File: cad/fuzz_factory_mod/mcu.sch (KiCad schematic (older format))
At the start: 3 parts

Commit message: Continued schematic.
Modified fuuz_factory circuit : use of matched transistor pairs.
Added USB interface, through FT230X and direct to MCU.
Associated footprints, except for XTAL and trimmers.
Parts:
- removed P? (x2): CONN_NUCLEO_L152RE, symbol flax_lib:CONN_NUCLEO_L152RE
- removed R?: R, symbol Device:R
- added C201, C209: 1u, Capacitors_SMD:C_0805, symbol Device:C
- added C202, C208: 10n, Capacitors_SMD:C_0603, symbol Device:C
- added C203: 4u7, Capacitors_SMD:C_1206, symbol Device:C
- added C204, C205, C206, C207: 100n, Capacitors_SMD:C_0603, symbol Device:C
- added J201: Conn_MCU_SWD, Pin_Headers:Pin_Header_Straight_1x07_Pitch2.54mm, symbol Connector:Conn_01x07_Male
- added L201: BLMxxx, Capacitors_SMD:C_0603, symbol Device:L
- added R201: 10k, Resistors_SMD:R_0603, symbol Device:R_Small
- added R202: 390, Resistors_SMD:R_0603, symbol Device:R_Small
- added R203: 1M, Resistors_SMD:R_0603, symbol Device:R_Small
- added U201: STM32F303VCTx, Housings_QFP:LQFP-100_14x14mm_Pitch0.5mm, symbol MCU_ST_STM32F3:STM32F303VCTx
- added Y201: Resonator_Small, symbol Device:Resonator_Small
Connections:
- net labels added: +3.3VA, ADC1_IN1, ADC1_IN2, ADC1_IN3, ADC1_IN4, ADC1_IN5, ADC2_IN5, ADC2_IN6, ADC2_IN7, ADC2_IN8, ADC2_IN9, ADC_FF_pol1, ADC_FF_pol2, ADC_FF_pol3, ADC_Peak_input, ADC_Peak_output, ADC_Ref_pol1, ADC_Ref_pol2, ADC_Ref_pol3, DAC_OUT1, ENC1_BTN, ENC1_IN_CCW, ENC1_IN_CW, ENC1_LED_BLUE, ENC1_LED_GREEN, ENC1_LED_RED, ENC2_BTN, ENC2_IN_CCW, ENC2_IN_CW, ENC2_LED_BLUE, ENC2_LED_GREEN, ENC2_LED_RED, FF_Stab_DAC_PWM, GNDA, JNTRST, JTCK_SWCLK, JTDI, JTDO_TRACESWO, JTMS_SWDIO, LED_BYPASS, LED_BYPASS_CMD, MUX1, MUX2, MUX3, Ref_Stab_DAC_PWM, SPI1_CS, SPI1_MISO, SPI1_MOSI, SPI1_SCK, SPI2_MISO, SPI2_MOSI, SPI2_NSS, SPI2_SCK, SPI3_MOSI, SPI3_SCK, SPI_FF_Gain_CS, SPI_FF_Gain_MISO, SPI_FF_Gain_MOSI, SPI_FF_Gain_SCK, SW_BYPASS, SW_PRESET_DOWN, SW_PRESET_UP, TIM1_CH1, TIM1_CH2, TIM3_CH1, TIM3_CH2, TIM4_CH1, UART3_RX, UART3_TX, UART5_RX, UART5_TX, USART1_RX, USB_DM, USB_DP, VCA_IN_PWM, VCA_OUT_PWM
- net labels removed: +5V, +9V
- wire segments 11 -> 131

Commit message: Continued schematic.
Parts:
- Y201: footprint (none) -> Pin_Headers:Pin_Header_Straight_1x03_Pitch2.54mm
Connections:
- net labels added: FF_Stab_DAC_PWM_LSB, FF_Stab_DAC_PWM_MSB, Ref_Stab_DAC_PWM_LSB, Ref_Stab_DAC_PWM_MSB, TIM1_CH3, TIM1_CH4
- net labels removed: FF_Stab_DAC_PWM, Ref_Stab_DAC_PWM
- wire segments 131 -> 145
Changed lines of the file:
@@
 $Descr A4 11693 8268
 encoding utf-8
-Sheet 2 22
+Sheet 2 26
 Title ""
 Date ""
@@
 F 0 "Y201" V 2645 2600 50  0000 C CNN
 F 1 "Resonator_Small" V 2736 2600 50  0000 C CNN
-F 2 "" H 2925 2650 50  0001 C CNN
+F 2 "Pin_Headers:Pin_Header_Straight_1x03_Pitch2.54mm" H 2925 2650 50  0001 C CNN
 F 3 "~" H 2925 2650 50  0001 C CNN
 	1    2950 2650
@@
 Text GLabel 2500 3550 0    50   Input ~ 0
 SW_PRESET_DOWN
-Text GLabel 2500 3850 0    50   Input ~ 0
-ENC1_LED_RED
-Text GLabel 2500 3950 0    50   Input ~ 0
-ENC1_LED_GREEN
-Text GLabel 2500 4050 0    50   Input ~ 0
-ENC1_LED_BLUE
-Text GLabel 2500 5450 0    50   Input ~ 0
-ENC2_LED_RED
-Text GLabel 2500 5550 0    50   Input ~ 0
-ENC2_LED_GREEN
-Text GLabel 2500 5650 0    50   Input ~ 0
-ENC2_LED_BLUE
-Text GLabel 2500 5750 0    50   Input ~ 0
-ENC2_BTN
-Text GLabel 2500 5850 0    50   Input ~ 0
-ENC2_IN_CW
-Text GLabel 6500 6550 2    50   Input ~ 0
-ENC1_IN_CW
-Text GLabel 6500 6650 2    50   Input ~ 0
-ENC1_IN_CCW
-Text GLabel 6500 6450 2    50   Input ~ 0
-ENC1_BTN
-Text GLabel 6500 4050 2    50   Input ~ 0
-ENC2_IN_CCW
 Text GLabel 2500 3650 0    50   Input ~ 0
 VCA_IN_PWM
@@
 VCA_OUT_PWM
 Text GLabel 2500 4350 0    50   Input ~ 0
-FF_Stab_DAC_PWM
-Text GLabel 2500 4550 0    50   Input ~ 0
-Ref_Stab_DAC_PWM
+FF_Stab_DAC_PWM_LSB
+Text GLabel 2500 4750 0    50   Input ~ 0
+Ref_Stab_DAC_PWM_LSB
 $Sheet
-S 9950 4250 800  300
+S 10200 5600 800  300
 U 5EB00B3E
 F0 "USB_UART" 50
 F1 "USB_UART.sch" 50
-F2 "USB_RXD" I L 9950 4350 50
-F3 "USB_TXD" I L 9950 4450 50
+F2 "USB_RXD" I L 10200 5700 50
+F3 "USB_TXD" I L 10200 5800 50
 $EndSheet
 $Sheet
-S 9950 3650 800  300
+S 10200 5000 800  300
 U 5EB591ED
 F0 "USB_DEV" 50
 F1 "USB_DEV.sch" 50
-F2 "USB_DM" I L 9950 3750 50
-F3 "USB_DP" I L 9950 3850 50
+F2 "USB_DM" I L 10200 5100 50
+F3 "USB_DP" I L 10200 5200 50
 $EndSheet
-Text GLabel 9800 3750 0    50   Input ~ 0
+Text GLabel 10050 5100 0    50   Input ~ 0
 USB_DM
-Text GLabel 9800 3850 0    50   Input ~ 0
+Text GLabel 10050 5200 0    50   Input ~ 0
 USB_DP
 Wire Wire Line
-	9800 3750 9950 3750
-Wire Wire Line
-	9950 3850 9800 3850
+	10050 5100 10200 5100
+Wire Wire Line
+	10200 5200 10050 5200
+Text Label 3650 4750 2    50   ~ 0
+TIM1_CH3
+Text Label 3650 4850 2    50   ~ 0
+TIM1_CH4
+Wire Wire Line
+	3750 4750 2500 4750
+Wire Wire Line
+	3750 4850 2500 4850
+Text GLabel 2500 4550 0    50   Input ~ 0
+FF_Stab_DAC_PWM_MSB
+Text GLabel 2500 4850 0    50   Input ~ 0
+Ref_Stab_DAC_PWM_MSB
+$Sheet
+S 10000 1500 1000 2500
+U 5EEFDD5E
+F0 "interface" 50
+F1 "interface.sch" 50
+F2 "DISP_CLK" I L 10000 1600 50
+F3 "DISP_DATA" I L 10000 1700 50
+F4 "DISP_ENABLE" I L 10000 1800 50
+F5 "DISP_LATCH" I L 10000 1900 50
+F6 "ENC1_SW" I L 10000 2050 50
+F7 "ENC1_LED1" I L 10000 2150 50
+F8 "ENC1_LED2" I L 10000 2250 50
+F9 "ENC1_ENC1" I L 10000 2350 50
+F10 "ENC1_ENC2" I L 10000 2450 50
+F11 "FSW_bypass" I L 10000 3700 50
+F12 "ENC2_SW" I L 10000 2600 50
+F13 "ENC2_LED1" I L 10000 2700 50
+F14 "ENC2_LED2" I L 10000 2800 50
+F15 "ENC2_ENC1" I L 10000 2900 50
+F16 "ENC2_ENC2" I L 10000 3000 50
+F17 "ENC3_SW" I L 10000 3150 50
+F18 "ENC3_LED1" I L 10000 3250 50
+F19 "ENC3_LED2" I L 10000 3350 50
+F20 "ENC3_ENC1" I L 10000 3450 50
+F21 "ENC3_ENC2" I L 10000 3550 50
+$EndSheet
+Text Label 9900 1600 2    50   ~ 0
+SPI2_SCK
+Text Label 9900 1700 2    50   ~ 0
+SPI2_MOSI
+Wire Wire Line
+	10000 1600 9500 1600
+Wire Wire Line
+	10000 1700 9500 1700
+Text Label 9900 2700 2    50   ~ 0
+ENC2_LED_RED
+Text Label 9900 2800 2    50   ~ 0
+ENC2_LED_GREEN
+Text Label 9900 2600 2    50   ~ 0
+ENC2_BTN
+Text Label 9900 2900 2    50   ~ 0
+ENC2_IN_CW
+Text Label 9900 2050 2    50   ~ 0
+ENC1_BTN
+Text Label 9900 2350 2    50   ~ 0
+ENC1_IN_CW
+Text Label 9900 2450 2    50   ~ 0
+ENC1_IN_CCW
+Text Label 9900 2150 2    50   ~ 0
+ENC1_LED_RED
+Text Label 9900 2250 2    50   ~ 0
+ENC1_LED_GREEN
+Text Label 9900 3000 2    50   ~ 0
+ENC2_IN_CCW
+Wire Wire Line
+	10000 2050 9500 2050
+Wire Wire Line
+	10000 2150 9500 2150
+Wire Wire Line
+	10000 2250 9500 2250
+Wire Wire Line
+	10000 2350 9500 2350
+Wire Wire Line
+	10000 2450 9500 2450
+Wire Wire Line
+	10000 2600 9500 2600
+Wire Wire Line
+	10000 2700 9500 2700
+Wire Wire Line
+	10000 2800 9500 2800
+Wire Wire Line
+	10000 2900 9500 2900
+Wire Wire Line
+	10000 3000 9500 3000
 $EndSCHEMATC

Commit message: Continued schematic.
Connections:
- net labels added: BYPASS_CMD
- net labels removed: LED_BYPASS, LED_BYPASS_CMD
- wire segments 145 -> 153
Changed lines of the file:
@@
 $Descr A4 11693 8268
 encoding utf-8
-Sheet 2 26
+Sheet 2 30
 Title ""
 Date ""
@@
 	6500 5450 5350 5450
 Text Label 3650 3250 2    50   ~ 0
-LED_BYPASS
+BYPASS_CMD
 Wire Wire Line
 	3750 3250 2500 3250
@@
 Text GLabel 6500 3450 2    50   Input ~ 0
 SPI_FF_Gain_CS
-Text GLabel 2500 3150 0    50   Input ~ 0
-SW_BYPASS
 Text GLabel 2500 3250 0    50   Input ~ 0
-LED_BYPASS_CMD
-Text GLabel 2500 3450 0    50   Input ~ 0
-SW_PRESET_UP
-Text GLabel 2500 3550 0    50   Input ~ 0
-SW_PRESET_DOWN
+BYPASS_CMD
 Text GLabel 2500 3650 0    50   Input ~ 0
 VCA_IN_PWM
@@
 Wire Wire Line
 	10000 3000 9500 3000
+$Sheet
+S 10000 4250 1000 500
+U 5ECAAB94
+F0 "MIDI" 50
+F1 "MIDI.sch" 50
+F2 "MIDI_IN" I L 10000 4350 50
+F3 "MIDI_OUT" I L 10000 4650 50
+$EndSheet
+Text Label 9900 4350 2    50   ~ 0
+UART5_RX
+Text Label 9900 4650 2    50   ~ 0
+UART5_TX
+Wire Wire Line
+	10000 4350 9500 4350
+Wire Wire Line
+	10000 4650 9500 4650
+$Sheet
+S 8300 4700 700  300
+U 5ED0E0D0
+F0 "btn_bypass" 50
+F1 "push_button.sch" 50
+F2 "BTN" I L 8300 4900 50
+F3 "VCC" I L 8300 4800 50
+$EndSheet
+$Comp
+L power:+3.3V #PWR0229
+U 1 1 5ED10A5A
+P 8200 4800
+F 0 "#PWR0229" H 8200 4650 50  0001 C CNN
+F 1 "+3.3V" V 8215 4928 50  0000 L CNN
+F 2 "" H 8200 4800 50  0001 C CNN
+F 3 "" H 8200 4800 50  0001 C CNN
+	1    8200 4800
+	0    -1   -1   0
+$EndComp
+Wire Wire Line
+	8300 4800 8200 4800
+Text Label 8200 4900 2    50   ~ 0
+SW_BYPASS
+Wire Wire Line
+	8300 4900 7800 4900
+Text Label 8200 5400 2    50   ~ 0
+SW_PRESET_UP
+$Sheet
+S 8300 5200 700  300
+U 5ED20AFC
+F0 "btn_preset_up" 50
+F1 "push_button.sch" 50
+F2 "BTN" I L 8300 5400 50
+F3 "VCC" I L 8300 5300 50
+$EndSheet
+$Sheet
+S 8300 5700 700  300
+U 5ED214FE
+F0 "btn_preset_down" 50
+F1 "push_button.sch" 50
+F2 "BTN" I L 8300 5900 50
+F3 "VCC" I L 8300 5800 50
+$EndSheet
+Text Label 8200 5900 2    50   ~ 0
+SW_PRESET_DOWN
+Wire Wire Line
+	8300 5400 7500 5400
+Wire Wire Line
+	8300 5900 7500 5900
+$Comp
+L power:+3.3V #PWR0230
+U 1 1 5ED48B6A
+P 8200 5300
+F 0 "#PWR0230" H 8200 5150 50  0001 C CNN
+F 1 "+3.3V" V 8215 5428 50  0000 L CNN
+F 2 "" H 8200 5300 50  0001 C CNN
+F 3 "" H 8200 5300 50  0001 C CNN
+	1    8200 5300
+	0    -1   -1   0
+$EndComp
+$Comp
+L power:+3.3V #PWR0231
+U 1 1 5ED48FD7
+P 8200 5800
+F 0 "#PWR0231" H 8200 5650 50  0001 C CNN
+F 1 "+3.3V" V 8215 5928 50  0000 L CNN
+F 2 "" H 8200 5800 50  0001 C CNN
+F 3 "" H 8200 5800 50  0001 C CNN
+	1    8200 5800
+	0    -1   -1   0
+$EndComp
+Wire Wire Line
+	8300 5800 8200 5800
+Wire Wire Line
+	8300 5300 8200 5300
 $EndSCHEMATC

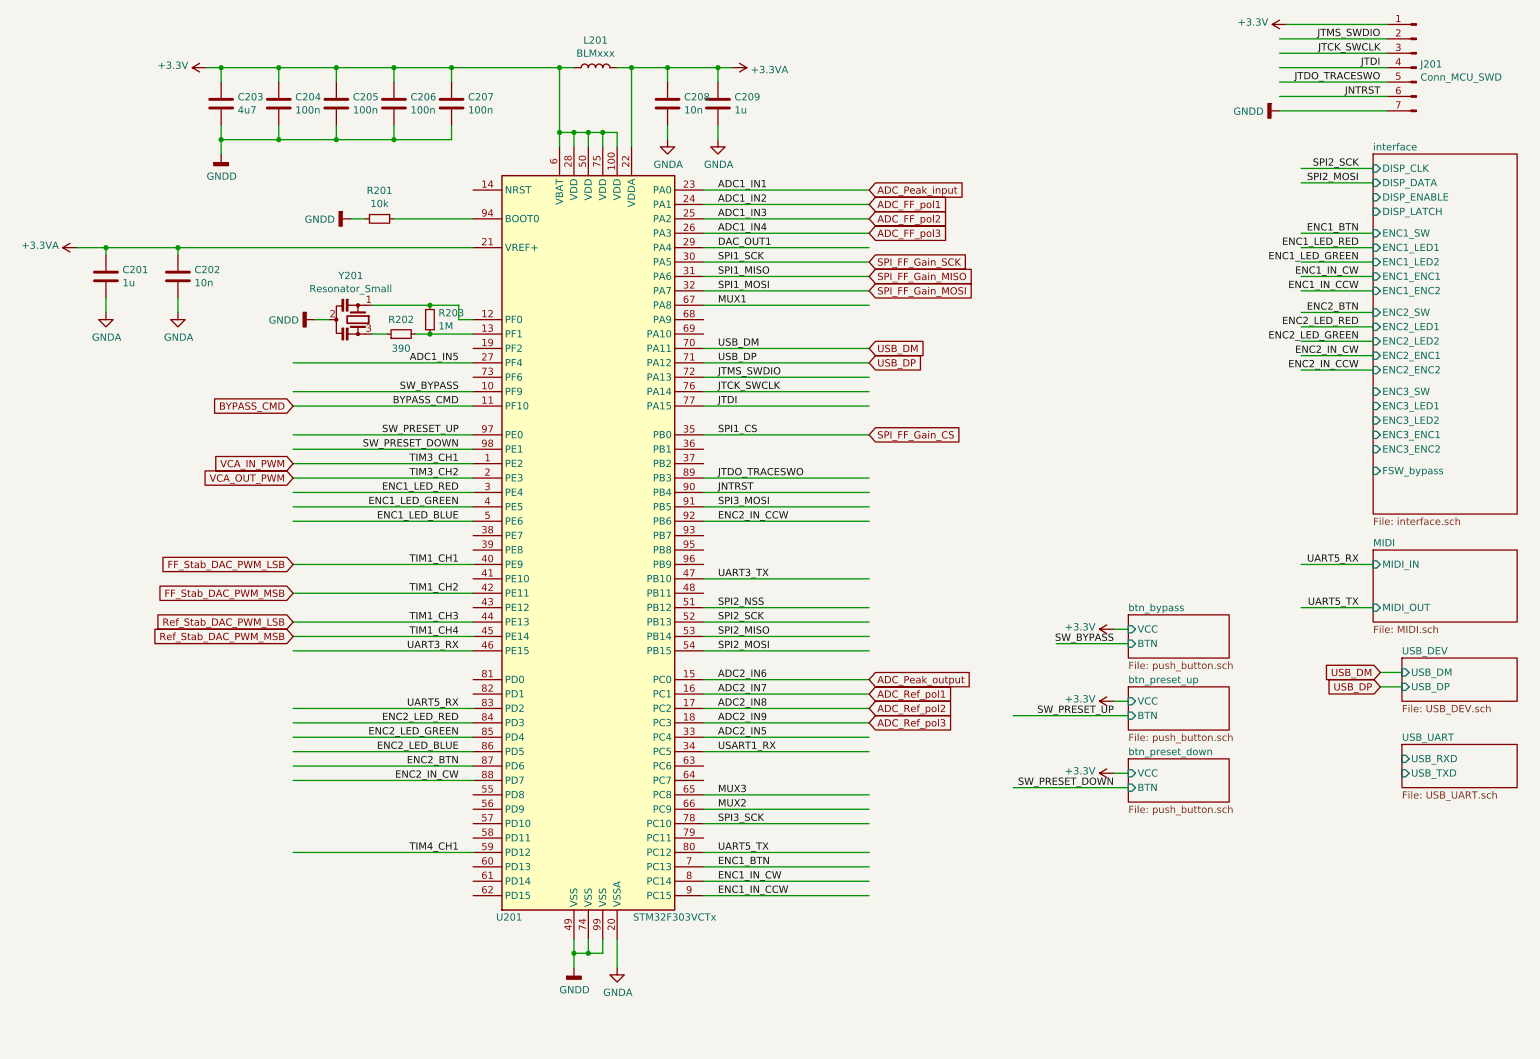
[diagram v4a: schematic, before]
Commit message: Continued schematic.
Continued component placement.
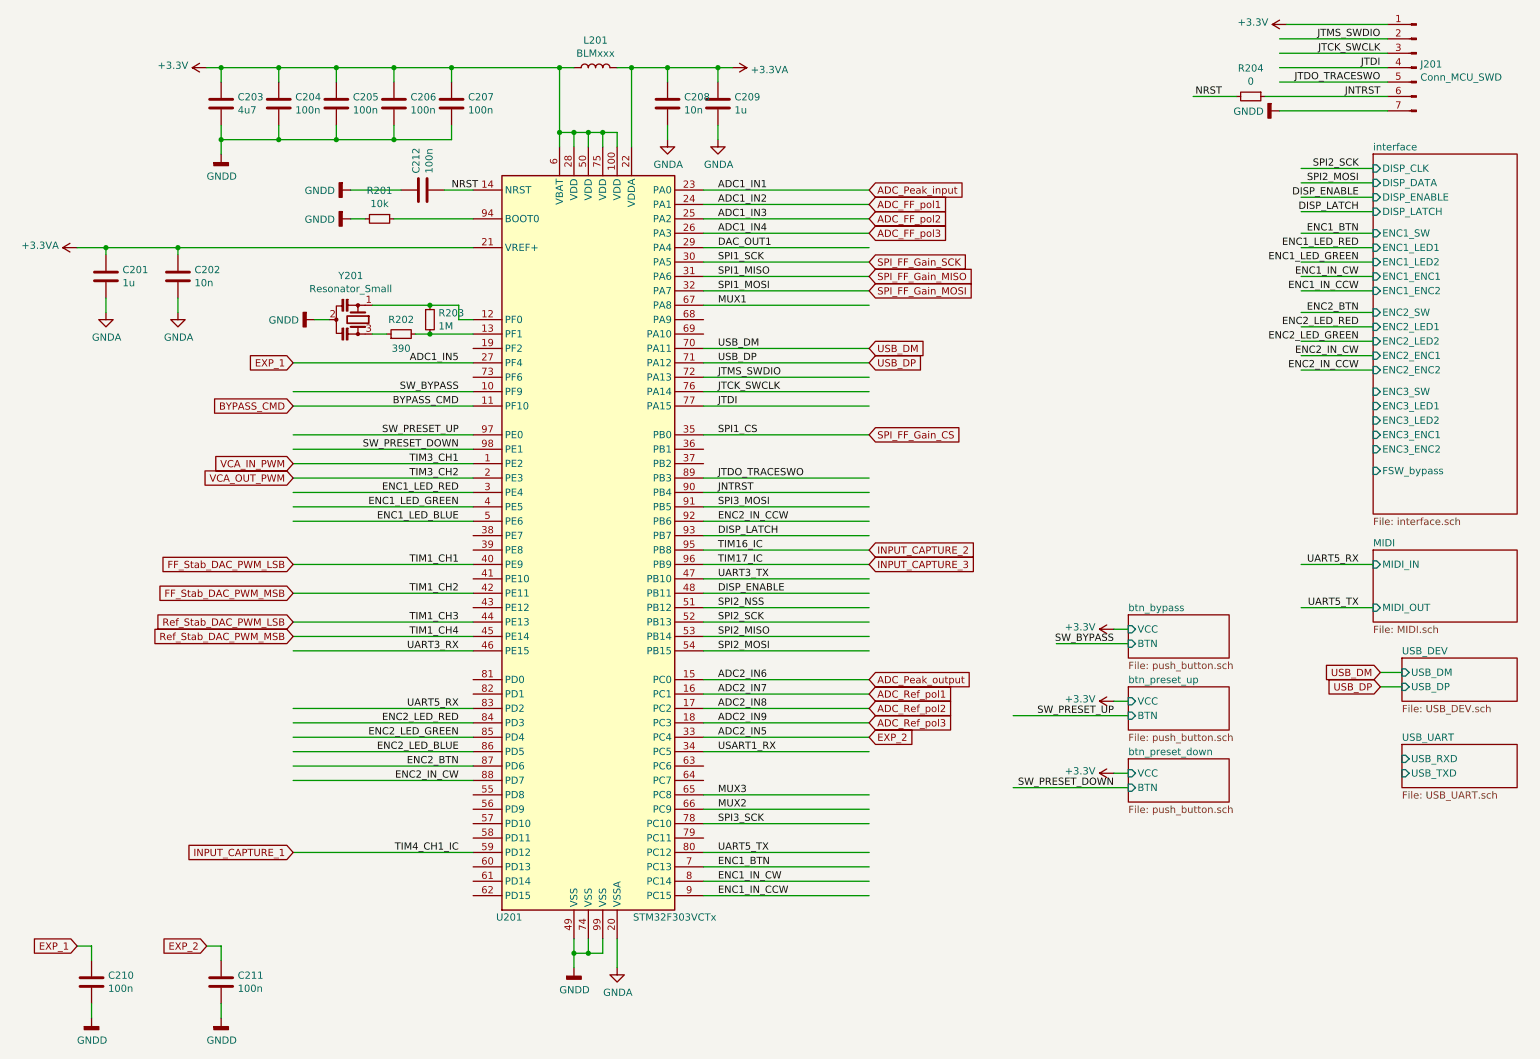
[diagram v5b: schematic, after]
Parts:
- added C210, C211, C212: 100n, Capacitors_SMD:C_0603, symbol Device:C
- added R204: 0, Resistors_SMD:R_0603, symbol Device:R_Small
- Y201: footprint Pin_Headers:Pin_Header_Straight_1x03_Pitch2.54mm -> flax_lib:Resonator_AEL_ZTTxx_SMD
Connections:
- net labels added: DISP_ENABLE, DISP_LATCH, EXP_1, EXP_2, INPUT_CAPTURE_1, INPUT_CAPTURE_2, INPUT_CAPTURE_3, NRST, TIM16_IC, TIM17_IC, TIM4_CH1_IC
- net labels removed: TIM4_CH1
- wire segments 153 -> 168
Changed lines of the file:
@@
 F 0 "Y201" V 2645 2600 50  0000 C CNN
 F 1 "Resonator_Small" V 2736 2600 50  0000 C CNN
-F 2 "Pin_Headers:Pin_Header_Straight_1x03_Pitch2.54mm" H 2925 2650 50  0001 C CNN
+F 2 "flax_lib:Resonator_AEL_ZTTxx_SMD" H 2925 2650 50  0001 C CNN
 F 3 "~" H 2925 2650 50  0001 C CNN
 	1    2950 2650
@@
 Wire Wire Line
 	9350 1200 10100 1200
-Wire Wire Line
-	10100 1100 9350 1100
 Wire Wire Line
 	10100 1000 9350 1000
@@
 	5350 2550 6500 2550
 Text Label 3650 6350 2    50   ~ 0
-TIM4_CH1
+TIM4_CH1_IC
 Wire Wire Line
 	3750 6350 2500 6350
@@
 Wire Wire Line
 	8300 5300 8200 5300
+Text GLabel 2500 2950 0    50   Input ~ 0
+EXP_1
+Text GLabel 6500 5550 2    50   Input ~ 0
+EXP_2
+Text GLabel 1000 7000 0    50   Input ~ 0
+EXP_1
+$Comp
+L Device:C C210
+U 1 1 5ECD3C8C
+P 1100 7250
+F 0 "C210" H 1215 7296 50  0000 L CNN
+F 1 "100n" H 1215 7205 50  0000 L CNN
+F 2 "Capacitors_SMD:C_0603" H 1138 7100 50  0001 C CNN
+F 3 "~" H 1100 7250 50  0001 C CNN
+	1    1100 7250
+	1    0    0    -1
+$EndComp
+$Comp
+L power:GNDD #PWR0232
+U 1 1 5ECD4C09
+P 1100 7500
+F 0 "#PWR0232" H 1100 7250 50  0001 C CNN
+F 1 "GNDD" H 1104 7345 50  0000 C CNN
+F 2 "" H 1100 7500 50  0001 C CNN
+F 3 "" H 1100 7500 50  0001 C CNN
+	1    1100 7500
+	1    0    0    -1
+$EndComp
+Wire Wire Line
+	1100 7400 1100 7500
+Wire Wire Line
+	1000 7000 1100 7000
+Wire Wire Line
+	1100 7000 1100 7100
+Text GLabel 1900 7000 0    50   Input ~ 0
+EXP_2
+$Comp
+L Device:C C211
+U 1 1 5ECE5D07
+P 2000 7250
+F 0 "C211" H 2115 7296 50  0000 L CNN
+F 1 "100n" H 2115 7205 50  0000 L CNN
+F 2 "Capacitors_SMD:C_0603" H 2038 7100 50  0001 C CNN
+F 3 "~" H 2000 7250 50  0001 C CNN
+	1    2000 7250
+	1    0    0    -1
+$EndComp
+$Comp
+L power:GNDD #PWR0247
+U 1 1 5ECE5D11
+P 2000 7500
+F 0 "#PWR0247" H 2000 7250 50  0001 C CNN
+F 1 "GNDD" H 2004 7345 50  0000 C CNN
+F 2 "" H 2000 7500 50  0001 C CNN
+F 3 "" H 2000 7500 50  0001 C CNN
+	1    2000 7500
+	1    0    0    -1
+$EndComp
+Wire Wire Line
+	2000 7400 2000 7500
+Wire Wire Line
+	1900 7000 2000 7000
+Wire Wire Line
+	2000 7000 2000 7100
+$Comp
+L Device:R_Small R204
+U 1 1 5ECF0FAA
+P 9150 1100
+F 0 "R204" V 8954 1100 50  0000 C CNN
+F 1 "0" V 9045 1100 50  0000 C CNN
+F 2 "Resistors_SMD:R_0603" H 9150 1100 50  0001 C CNN
+F 3 "~" H 9150 1100 50  0001 C CNN
+	1    9150 1100
+	0    1    1    0
+$EndComp
+Wire Wire Line
+	3550 1750 3750 1750
+Text Label 3600 1750 0    50   ~ 0
+NRST
+Wire Wire Line
+	9250 1100 10100 1100
+Text Label 8950 1100 2    50   ~ 0
+NRST
+Wire Wire Line
+	9050 1100 8750 1100
+$Comp
+L Device:C C212
+U 1 1 5ED19030
+P 3400 1750
+F 0 "C212" H 3515 1796 50  0000 L CNN
+F 1 "100n" H 3515 1705 50  0000 L CNN
+F 2 "Capacitors_SMD:C_0603" H 3438 1600 50  0001 C CNN
+F 3 "~" H 3400 1750 50  0001 C CNN
+	1    3400 1750
+	0    -1   -1   0
+$EndComp
+$Comp
+L power:GNDD #PWR0248
+U 1 1 5ED19914
+P 2900 1750
+F 0 "#PWR0248" H 2900 1500 50  0001 C CNN
+F 1 "GNDD" V 2904 1640 50  0000 R CNN
+F 2 "" H 2900 1750 50  0001 C CNN
+F 3 "" H 2900 1750 50  0001 C CNN
+	1    2900 1750
+	0    1    1    0
+$EndComp
+Wire Wire Line
+	3250 1750 2900 1750
+Text Label 5450 4550 0    50   ~ 0
+DISP_ENABLE
+Wire Wire Line
+	5350 4550 6500 4550
+Text Label 5450 4150 0    50   ~ 0
+DISP_LATCH
+Text Label 9900 1900 2    50   ~ 0
+DISP_LATCH
+Text Label 9900 1800 2    50   ~ 0
+DISP_ENABLE
+Wire Wire Line
+	10000 1800 9500 1800
+Wire Wire Line
+	10000 1900 9500 1900
+Wire Wire Line
+	5350 4150 6500 4150
+Text Label 5450 4250 0    50   ~ 0
+TIM16_IC
+Text Label 5450 4350 0    50   ~ 0
+TIM17_IC
+Wire Wire Line
+	5350 4250 6500 4250
+Wire Wire Line
+	5350 4350 6500 4350
+Text GLabel 2500 6350 0    50   Input ~ 0
+INPUT_CAPTURE_1
+Text GLabel 6500 4250 2    50   Input ~ 0
+INPUT_CAPTURE_2
+Text GLabel 6500 4350 2    50   Input ~ 0
+INPUT_CAPTURE_3
 $EndSCHEMATC
